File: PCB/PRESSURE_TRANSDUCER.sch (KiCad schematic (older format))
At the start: 3 parts, among them U3 MPRLF0006KG00001C

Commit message: Added Dielectric and voltage rating to all capacitors
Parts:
- C19, C20: Dielectric (none) -> X7R; Voltage Rating (none) -> 6.3V
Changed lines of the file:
@@
 $Descr A4 11693 8268
 encoding utf-8
-Sheet 9 20
+Sheet 7 20
 Title ""
 Date ""
@@
 F 2 "" H 6700 4150 50  0001 C CNN
 F 3 "" H 6700 4150 50  0001 C CNN
+F 4 "X7R" H 6700 4150 50  0001 C CNN "Dielectric"
+F 5 "6.3V" H 6700 4150 50  0001 C CNN "Voltage Rating"
 	1    6700 4150
 	1    0    0    -1
@@
 F 2 "" H 5950 2850 50  0001 C CNN
 F 3 "" H 5950 2850 50  0001 C CNN
+F 4 "X7R" H 5950 2850 50  0001 C CNN "Dielectric"
+F 5 "6.3V" H 5950 2850 50  0001 C CNN "Voltage Rating"
 	1    5950 2850
 	1    0    0    -1

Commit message: Added some footprints
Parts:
- U3: footprint (none) -> custom:MPRxxxxxxxxxxxxxx
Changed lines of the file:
@@
 F 0 "U3" H 5600 4600 50  0000 C CNN
 F 1 "MPRLF0006KG00001C" H 6400 4600 50  0000 C CNN
-F 2 "" H 5950 4150 50  0001 C CNN
+F 2 "custom:MPRxxxxxxxxxxxxxx" H 5950 4150 50  0001 C CNN
 F 3 "https://sensing.honeywell.com/honeywell-sensing-micropressure-board-mount-pressure-mpr-series-datasheet-32332628.pdf" H 5950 4150 50  0001 C CNN
 	1    5950 4150

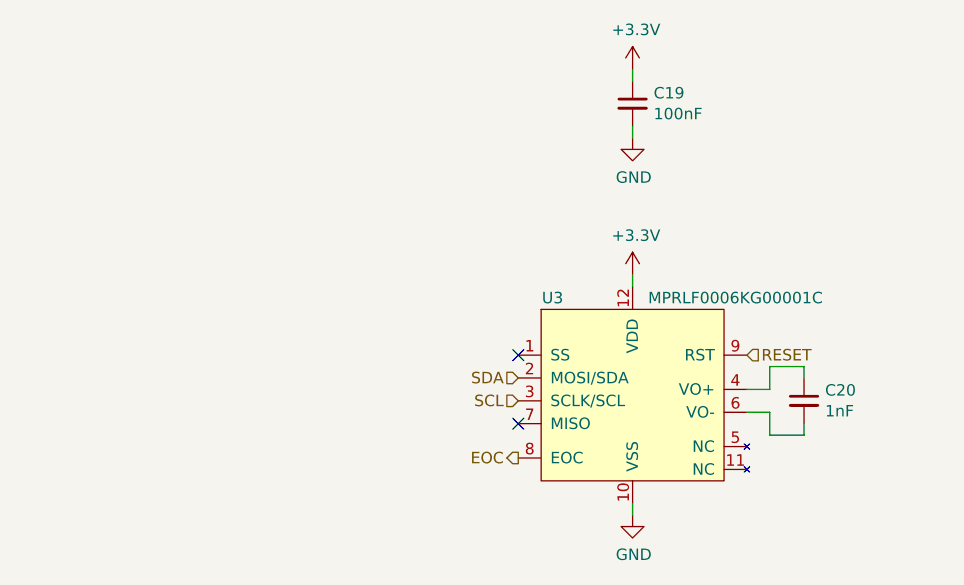
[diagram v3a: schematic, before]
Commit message: Added differential pressure and level shifter for gauge pressure sensor
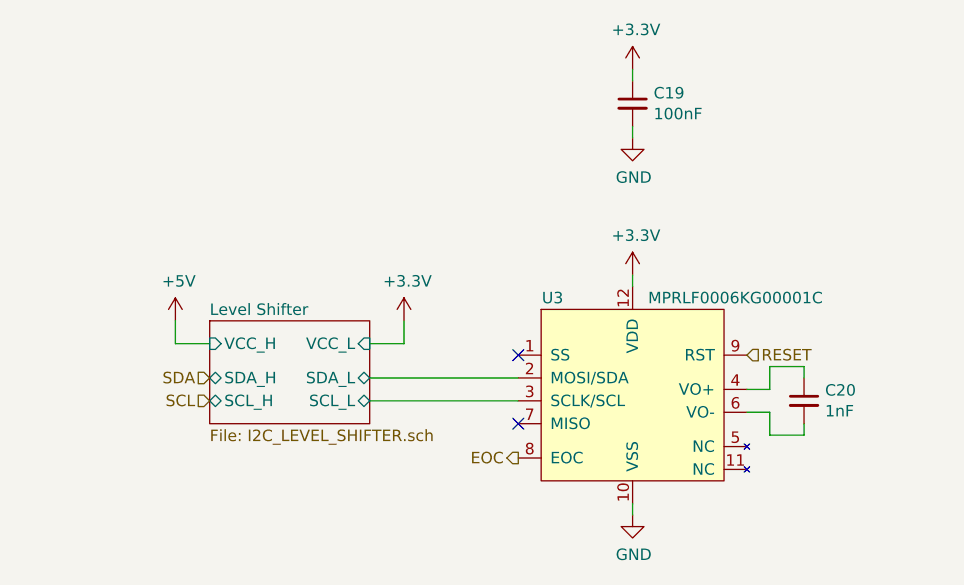
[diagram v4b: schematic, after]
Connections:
- net SCL: no longer U3.3 (SCLK/SCL)
- net SDA: no longer U3.2 (MOSI/SDA)
- new net Level Shifter/SCL_L: U3.3 (SCLK/SCL)
- new net Level Shifter/SDA_L: U3.2 (MOSI/SDA)
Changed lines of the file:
@@
 $Descr A4 11693 8268
 encoding utf-8
-Sheet 7 21
+Sheet 7 25
 Title ""
 Date ""
@@
 EOC
 NoConn ~ 5450 4250
-Text HLabel 5450 4150 0    50   Input ~ 0
+Text HLabel 4100 4150 0    50   Input ~ 0
 SCL
-Text HLabel 5450 4050 0    50   Input ~ 0
+Text HLabel 4100 4050 0    50   Input ~ 0
 SDA
 NoConn ~ 5450 3950
+$Sheet
+S 4100 3800 700  450
+U 5E8E2D5E
+F0 "Level Shifter" 50
+F1 "I2C_LEVEL_SHIFTER.sch" 50
+F2 "SDA_L" B R 4800 4050 50
+F3 "SCL_L" B R 4800 4150 50
+F4 "SDA_H" B L 4100 4050 50
+F5 "SCL_H" B L 4100 4150 50
+F6 "VCC_H" I L 4100 3900 50
+F7 "VCC_L" I R 4800 3900 50
+$EndSheet
+Wire Wire Line
+	4800 4050 5450 4050
+Wire Wire Line
+	4800 4150 5450 4150
+$Comp
+L power:+3.3V #PWR?
+U 1 1 5E8F8A8D
+P 4950 3800
+F 0 "#PWR?" H 4950 3650 50  0001 C CNN
+F 1 "+3.3V" H 4965 3973 50  0000 C CNN
+F 2 "" H 4950 3800 50  0001 C CNN
+F 3 "" H 4950 3800 50  0001 C CNN
+	1    4950 3800
+	1    0    0    -1
+$EndComp
+Wire Wire Line
+	4800 3900 4950 3900
+Wire Wire Line
+	4950 3900 4950 3800
+$Comp
+L power:+5V #PWR?
+U 1 1 5E8F9AC2
+P 3950 3800
+F 0 "#PWR?" H 3950 3650 50  0001 C CNN
+F 1 "+5V" H 3965 3973 50  0000 C CNN
+F 2 "" H 3950 3800 50  0001 C CNN
+F 3 "" H 3950 3800 50  0001 C CNN
+	1    3950 3800
+	1    0    0    -1
+$EndComp
+Wire Wire Line
+	3950 3800 3950 3900
+Wire Wire Line
+	3950 3900 4100 3900
 $EndSCHEMATC

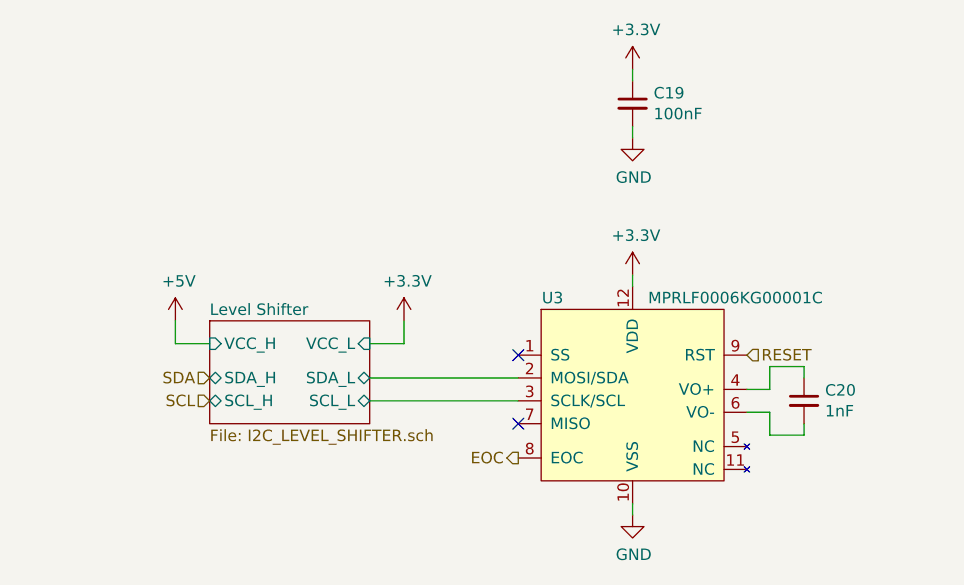
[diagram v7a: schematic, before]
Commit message: Added test points to sensors
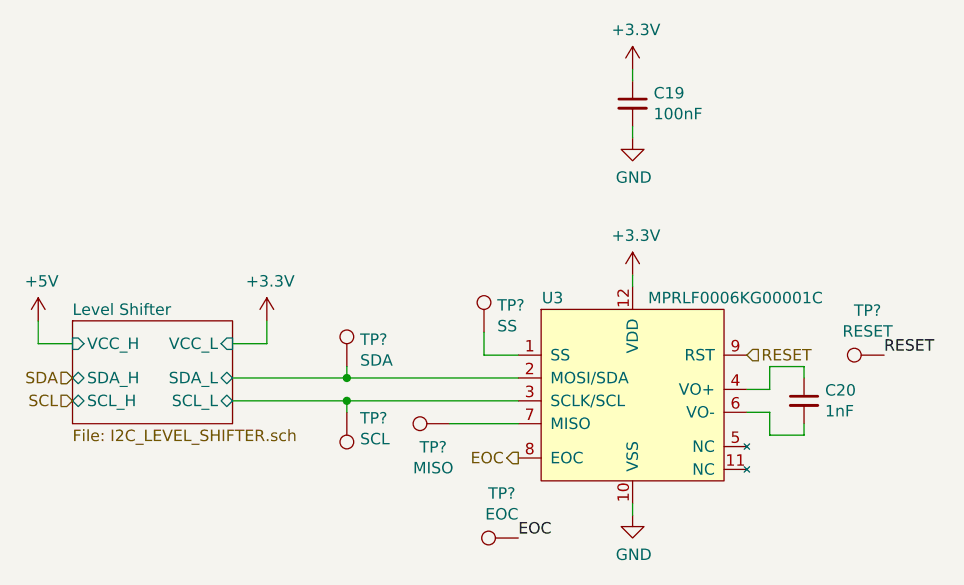
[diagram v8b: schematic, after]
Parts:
- added TP?: SS, symbol Connector:TestPoint
- added TP?: MISO, symbol Connector:TestPoint
- added TP?: EOC, symbol Connector:TestPoint
- added TP?: RESET, symbol Connector:TestPoint
- added TP?: SDA, symbol Connector:TestPoint
- added TP?: SCL, symbol Connector:TestPoint
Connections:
- net EOC: now also TP?.1
- net Level Shifter/SCL_L: now also TP?.1
- net Level Shifter/SDA_L: now also TP?.1
- net RESET: now also TP?.1
- net at U3.1 (SS): now also TP?.1
- net at U3.7 (MISO): now also TP?.1
- no-connect marks 2 -> 0
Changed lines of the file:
@@
 $EndDescr
-$Comp
-L custom:MPRxxxxxxxxxxxxxx U3
-U 1 1 5E870004
-P 5950 4150
-F 0 "U3" H 5600 4600 50  0000 C CNN
-F 1 "MPRLF0006KG00001C" H 6400 4600 50  0000 C CNN
-F 2 "custom:MPRxxxxxxxxxxxxxx" H 5950 4150 50  0001 C CNN
-F 3 "https://sensing.honeywell.com/honeywell-sensing-micropressure-board-mount-pressure-mpr-series-datasheet-32332628.pdf" H 5950 4150 50  0001 C CNN
-	1    5950 4150
-	1    0    0    -1
-$EndComp
 $Comp
 L power:+3.3V #PWR060
@@
 Text HLabel 5450 4400 0    50   Output ~ 0
 EOC
-NoConn ~ 5450 4250
-Text HLabel 4100 4150 0    50   Input ~ 0
+Text HLabel 3500 4150 0    50   Input ~ 0
 SCL
-Text HLabel 4100 4050 0    50   Input ~ 0
+Text HLabel 3500 4050 0    50   Input ~ 0
 SDA
-NoConn ~ 5450 3950
 $Sheet
-S 4100 3800 700  450
+S 3500 3800 700  450
 U 5E8E2D5E
 F0 "Level Shifter" 50
 F1 "I2C_LEVEL_SHIFTER.sch" 50
-F2 "SDA_L" B R 4800 4050 50
-F3 "SCL_L" B R 4800 4150 50
-F4 "SDA_H" B L 4100 4050 50
-F5 "SCL_H" B L 4100 4150 50
-F6 "VCC_H" I L 4100 3900 50
-F7 "VCC_L" I R 4800 3900 50
+F2 "SDA_L" B R 4200 4050 50
+F3 "SCL_L" B R 4200 4150 50
+F4 "SDA_H" B L 3500 4050 50
+F5 "SCL_H" B L 3500 4150 50
+F6 "VCC_H" I L 3500 3900 50
+F7 "VCC_L" I R 4200 3900 50
 $EndSheet
 Wire Wire Line
-	4800 4050 5450 4050
-Wire Wire Line
-	4800 4150 5450 4150
+	4200 4050 4700 4050
+Wire Wire Line
+	4200 4150 4700 4150
 $Comp
 L power:+3.3V #PWR057
 U 1 1 5E8F8A8D
-P 4950 3800
-F 0 "#PWR057" H 4950 3650 50  0001 C CNN
-F 1 "+3.3V" H 4965 3973 50  0000 C CNN
-F 2 "" H 4950 3800 50  0001 C CNN
-F 3 "" H 4950 3800 50  0001 C CNN
-	1    4950 3800
-	1    0    0    -1
-$EndComp
-Wire Wire Line
-	4800 3900 4950 3900
-Wire Wire Line
-	4950 3900 4950 3800
+P 4350 3800
+F 0 "#PWR057" H 4350 3650 50  0001 C CNN
+F 1 "+3.3V" H 4365 3973 50  0000 C CNN
+F 2 "" H 4350 3800 50  0001 C CNN
+F 3 "" H 4350 3800 50  0001 C CNN
+	1    4350 3800
+	1    0    0    -1
+$EndComp
+Wire Wire Line
+	4200 3900 4350 3900
+Wire Wire Line
+	4350 3900 4350 3800
 $Comp
 L power:+5V #PWR056
 U 1 1 5E8F9AC2
-P 3950 3800
-F 0 "#PWR056" H 3950 3650 50  0001 C CNN
-F 1 "+5V" H 3965 3973 50  0000 C CNN
-F 2 "" H 3950 3800 50  0001 C CNN
-F 3 "" H 3950 3800 50  0001 C CNN
-	1    3950 3800
-	1    0    0    -1
-$EndComp
-Wire Wire Line
-	3950 3800 3950 3900
-Wire Wire Line
-	3950 3900 4100 3900
+P 3350 3800
+F 0 "#PWR056" H 3350 3650 50  0001 C CNN
+F 1 "+5V" H 3365 3973 50  0000 C CNN
+F 2 "" H 3350 3800 50  0001 C CNN
+F 3 "" H 3350 3800 50  0001 C CNN
+	1    3350 3800
+	1    0    0    -1
+$EndComp
+Wire Wire Line
+	3350 3800 3350 3900
+Wire Wire Line
+	3350 3900 3500 3900
+$Comp
+L Connector:TestPoint TP?
+U 1 1 5E9246E8
+P 5300 3850
+AR Path="/5E9246E8" Ref="TP?"  Part="1"
+AR Path="/5E86C5C8/5E9246E8" Ref="TP?"  Part="1"
+F 0 "TP?" H 5358 3968 50  0000 L CNN
+F 1 "SS" H 5358 3877 50  0000 L CNN
+F 2 "" H 5500 3850 50  0001 C CNN
+F 3 "~" H 5500 3850 50  0001 C CNN
+	1    5300 3850
+	1    0    0    -1
+$EndComp
+$Comp
+L Connector:TestPoint TP?
+U 1 1 5E92531E
+P 5150 4250
+AR Path="/5E92531E" Ref="TP?"  Part="1"
+AR Path="/5E86C5C8/5E92531E" Ref="TP?"  Part="1"
+F 0 "TP?" V 5047 4322 50  0000 C CNN
+F 1 "MISO" V 4956 4322 50  0000 C CNN
+F 2 "" H 5350 4250 50  0001 C CNN
+F 3 "~" H 5350 4250 50  0001 C CNN
+	1    5150 4250
+	0    -1   -1   0
+$EndComp
+$Comp
+L Connector:TestPoint TP?
+U 1 1 5E9256B4
+P 5450 4750
+AR Path="/5E9256B4" Ref="TP?"  Part="1"
+AR Path="/5E86C5C8/5E9256B4" Ref="TP?"  Part="1"
+F 0 "TP?" V 5645 4822 50  0000 C CNN
+F 1 "EOC" V 5554 4822 50  0000 C CNN
+F 2 "" H 5650 4750 50  0001 C CNN
+F 3 "~" H 5650 4750 50  0001 C CNN
+	1    5450 4750
+	0    -1   -1   0
+$EndComp
+$Comp
+L Connector:TestPoint TP?
+U 1 1 5E925A1B
+P 7050 3950
+AR Path="/5E925A1B" Ref="TP?"  Part="1"
+AR Path="/5E86C5C8/5E925A1B" Ref="TP?"  Part="1"
+F 0 "TP?" V 7245 4022 50  0000 C CNN
+F 1 "RESET" V 7154 4022 50  0000 C CNN
+F 2 "" H 7250 3950 50  0001 C CNN
+F 3 "~" H 7250 3950 50  0001 C CNN
+	1    7050 3950
+	0    -1   -1   0
+$EndComp
+$Comp
+L custom:MPRxxxxxxxxxxxxxx U3
+U 1 1 5E870004
+P 5950 4150
+F 0 "U3" H 5600 4600 50  0000 C CNN
+F 1 "MPRLF0006KG00001C" H 6400 4600 50  0000 C CNN
+F 2 "custom:MPRxxxxxxxxxxxxxx" H 5950 4150 50  0001 C CNN
+F 3 "https://sensing.honeywell.com/honeywell-sensing-micropressure-board-mount-pressure-mpr-series-datasheet-32332628.pdf" H 5950 4150 50  0001 C CNN
+	1    5950 4150
+	1    0    0    -1
+$EndComp
+Wire Wire Line
+	5300 3850 5300 3950
+Wire Wire Line
+	5300 3950 5450 3950
+Wire Wire Line
+	5150 4250 5450 4250
+Text Label 5450 4750 0    50   ~ 0
+EOC
+Text Label 7050 3950 0    50   ~ 0
+RESET
+$Comp
+L Connector:TestPoint TP?
+U 1 1 5E933055
+P 4700 4000
+AR Path="/5E933055" Ref="TP?"  Part="1"
+AR Path="/5E86C5C8/5E933055" Ref="TP?"  Part="1"
+F 0 "TP?" H 4758 4118 50  0000 L CNN
+F 1 "SDA" H 4758 4027 50  0000 L CNN
+F 2 "" H 4900 4000 50  0001 C CNN
+F 3 "~" H 4900 4000 50  0001 C CNN
+	1    4700 4000
+	1    0    0    -1
+$EndComp
+$Comp
+L Connector:TestPoint TP?
+U 1 1 5E933539
+P 4700 4200
+AR Path="/5E933539" Ref="TP?"  Part="1"
+AR Path="/5E86C5C8/5E933539" Ref="TP?"  Part="1"
+F 0 "TP?" H 4642 4226 50  0000 R CNN
+F 1 "SCL" H 4642 4317 50  0000 R CNN
+F 2 "" H 4900 4200 50  0001 C CNN
+F 3 "~" H 4900 4200 50  0001 C CNN
+	1    4700 4200
+	-1   0    0    1
+$EndComp
+Wire Wire Line
+	4700 4000 4700 4050
+Connection ~ 4700 4050
+Wire Wire Line
+	4700 4050 5450 4050
+Wire Wire Line
+	4700 4200 4700 4150
+Connection ~ 4700 4150
+Wire Wire Line
+	4700 4150 5450 4150
 $EndSCHEMATC
